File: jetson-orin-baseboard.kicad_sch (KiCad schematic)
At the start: 0 parts

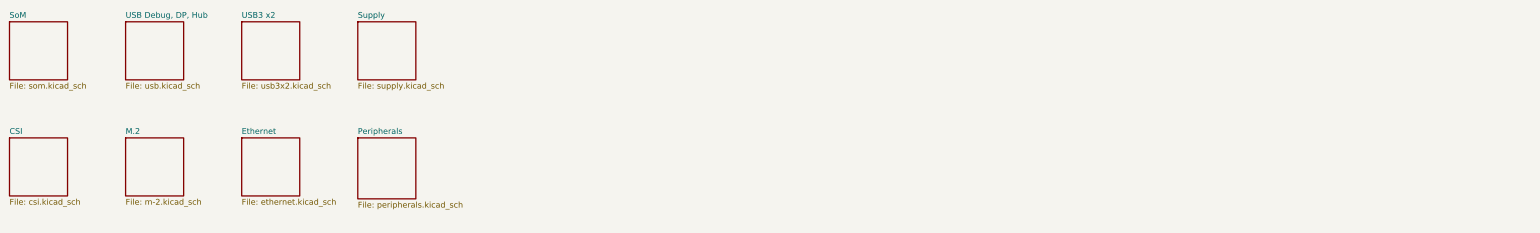
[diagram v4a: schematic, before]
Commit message: Remove USB connector, remove one M.2 key M, remove 40pin connector
Major changes to the design:
 - remove the USB 2.0 mux
 - remove one USB-C connectors
 - connect USB2-2 directly to the M.2 key E
 - remove one M.2 key M connectors
 - remove 40pin 2.54mm connector
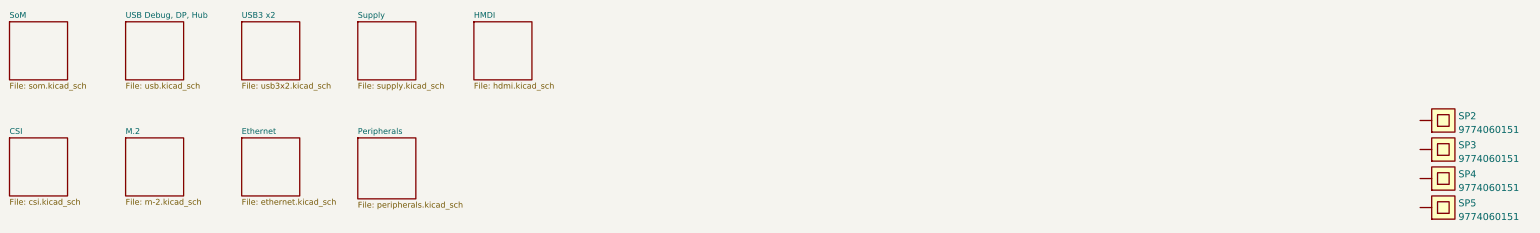
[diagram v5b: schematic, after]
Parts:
- added SP2, SP3, SP4, SP5: 9774060151, antmicro-footprints:9774060151, symbol antmicroMechanicalParts:9774060151
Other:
- added sheet HMDI (hdmi.kicad_sch)

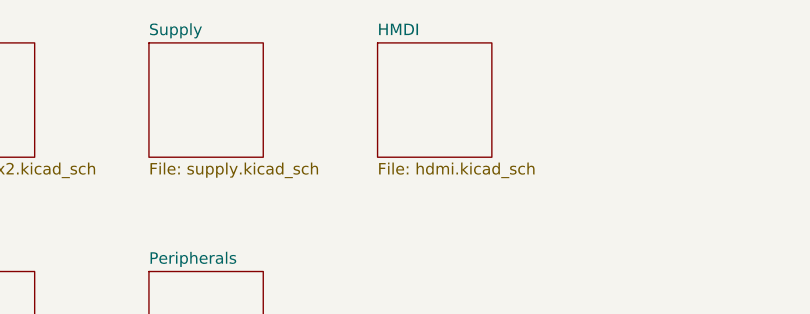
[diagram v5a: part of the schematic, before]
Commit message: Fix HDMI sheet name typo, GND symbols autoannotated
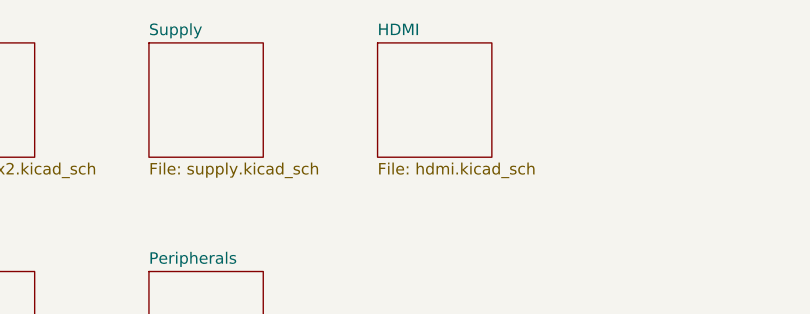
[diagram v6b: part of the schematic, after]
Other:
- sheet HMDI renamed HDMI
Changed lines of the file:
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@@
     (stroke (width 0.1524) (type solid) (color 0 0 0 0))
     (fill (color 0 0 0 0.0000))
-    (property "Sheet name" "HMDI" (id 0) (at 177.8 202.4884 0)
+    (property "Sheet name" "HDMI" (id 0) (at 177.8 202.4884 0)
       (effects (font (size 1.27 1.27)) (justify left bottom))
     )

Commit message: SCH: Update title block, set revision to 1.0.0
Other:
- title: Jetson Orin NX Baseboard -> Jetson Orin Baseboard
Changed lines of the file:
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@@
   (paper "A3")
   (title_block
-    (title "Jetson Orin NX Baseboard")
-    (date "2022-09-28")
-    (rev "0.1.0")
+    (title "Jetson Orin Baseboard")
+    (date "2022-09-29")
+    (rev "1.0.0")
     (company "Antmicro Ltd")
     (comment 1 "www.antmicro.com")

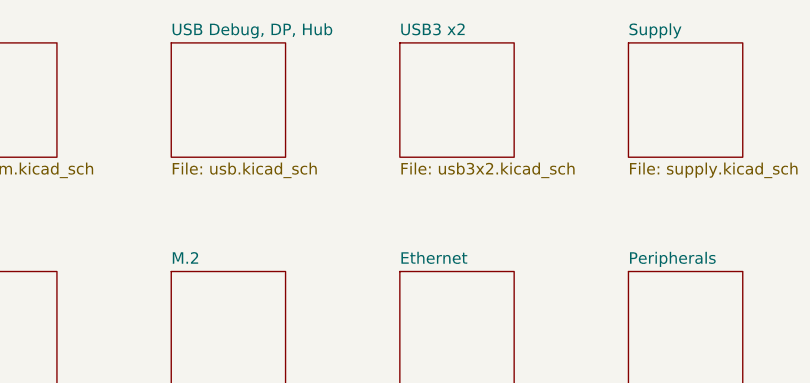
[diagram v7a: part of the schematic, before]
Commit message: Cleaned up schematic after project changes
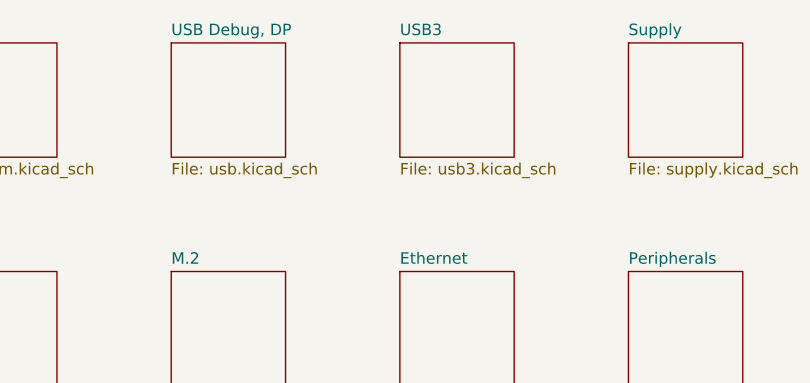
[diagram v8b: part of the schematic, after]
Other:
- sheet USB Debug, DP, Hub renamed USB Debug, DP
- sheet USB3 x2 renamed USB3
- sheet USB3: file usb3x2.kicad_sch -> usb3.kicad_sch
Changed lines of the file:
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@@
     (stroke (width 0.1524) (type solid) (color 0 0 0 0))
     (fill (color 0 0 0 0.0000))
-    (property "Sheet name" "USB3 x2" (id 0) (at 127 202.4884 0)
+    (property "Sheet name" "USB3" (id 0) (at 127 202.4884 0)
       (effects (font (size 1.27 1.27)) (justify left bottom))
     )
-    (property "Sheet file" "usb3x2.kicad_sch" (id 1) (at 127 216.4846 0)
+    (property "Sheet file" "usb3.kicad_sch" (id 1) (at 127 216.4846 0)
       (effects (font (size 1.27 1.27)) (justify left top))
     )
@@
     (stroke (width 0.1524) (type solid) (color 0 0 0 0))
     (fill (color 0 0 0 0.0000))
-    (property "Sheet name" "USB Debug, DP, Hub" (id 0) (at 101.6 202.4884 0)
+    (property "Sheet name" "USB Debug, DP" (id 0) (at 101.6 202.4884 0)
       (effects (font (size 1.27 1.27)) (justify left bottom))
     )
